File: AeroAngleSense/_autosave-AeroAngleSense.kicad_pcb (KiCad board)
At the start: 2 copper layers, 15 x 42 mm, 20 parts, among them IC1 STM32F042F6P6, IC2 TMP127EDBVRQ1, IC3 TPS62842DGRR, J1 SM06B-GHS-TBT, J7 SM04B-GHS-TBT

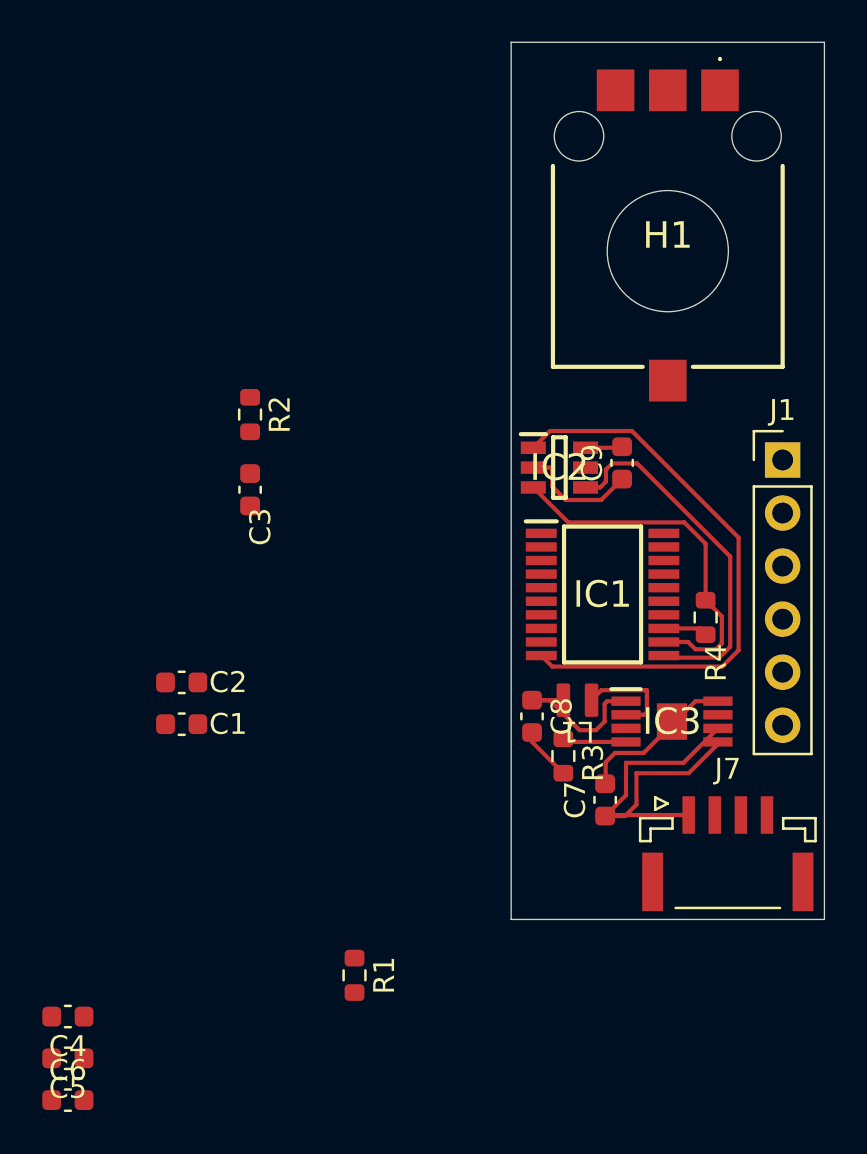
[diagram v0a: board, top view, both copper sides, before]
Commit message: 배선 연결 작업_1
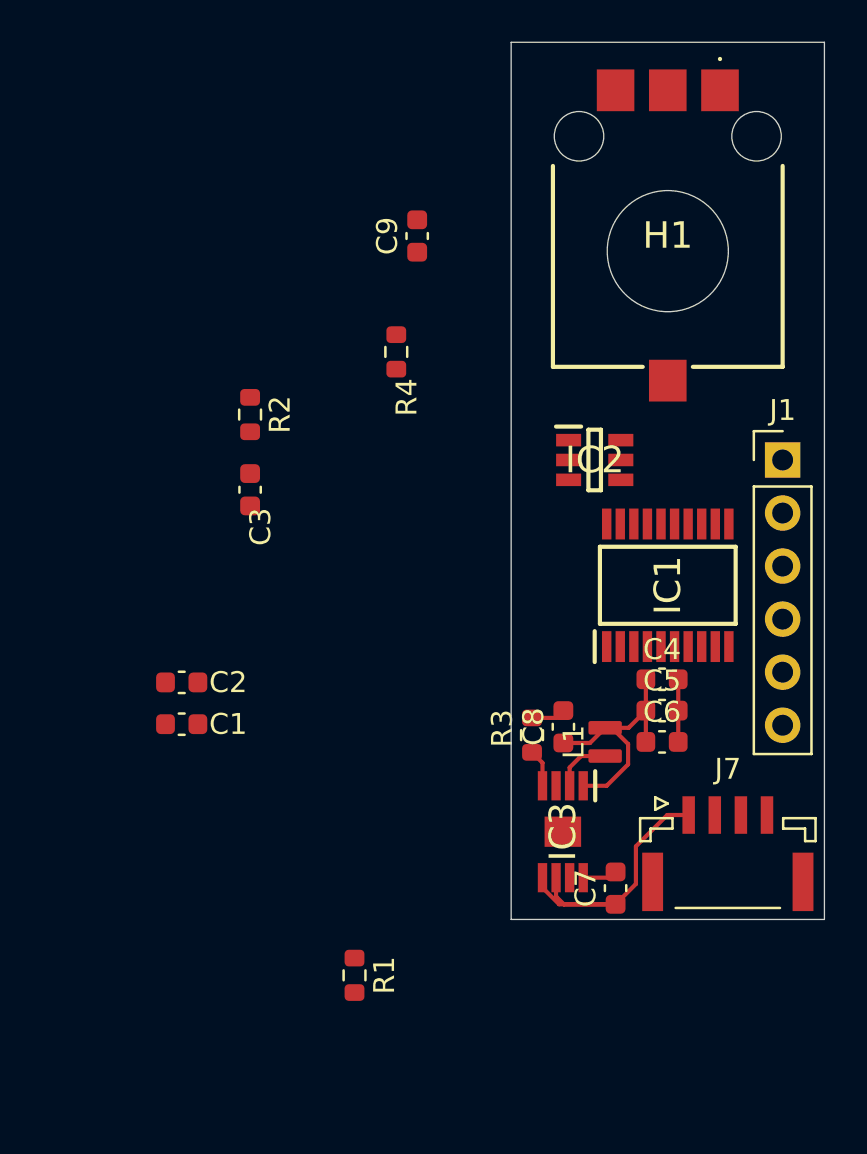
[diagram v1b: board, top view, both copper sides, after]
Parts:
- moved C6 33.2 mm to (66.7, 46.5)
- moved C5 33.0 mm to (66.7, 45.0), turned to 0 degrees
- moved C4 32.7 mm to (66.7, 43.5), turned to 0 degrees
- moved R4 19.5 mm to (54.0, 27.8)
- moved C9 14.6 mm to (55.0, 22.3)
- moved IC3 7.42 mm to (62.0, 50.8), turned to -90 degrees
- moved C7 4.25 mm to (64.5, 53.5)
- moved IC1 3.15 mm to (67.0, 39.0), turned to 90 degrees
- moved L1 2.40 mm to (64.0, 46.5), turned to 90 degrees
- moved R3 1.80 mm to (60.5, 46.2), turned to 90 degrees
- moved IC2 1.73 mm to (63.5, 33.0)
- moved C8 1.58 mm to (62.0, 45.8), turned to 90 degrees
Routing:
- net /TMP_CS: track 27.7 -> 0.00 mm
- net /TMP_MISO: track 17.5 -> 0.00 mm
- net /TMP_SCLK: track 17.3 -> 0.00 mm
- net GND: track 16.0 -> 6.31 mm
- net +5V: track 19.9 -> 14.5 mm
- net +3.3V: track 9.51 -> 12.6 mm
- net Net-(IC3-SW): track 4.95 -> 2.80 mm
- net /TMP_MOSI: track 2.12 -> 0.00 mm
- net Net-(IC3-VSET): track 3.06 -> 1.81 mm
